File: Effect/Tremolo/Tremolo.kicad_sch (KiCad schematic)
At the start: 20 parts, among them J1 Conn_01x03_Pin, J2 Conn_01x03_Pin, Q1 PMV250, Q2 PMV250, U1 OPA1655

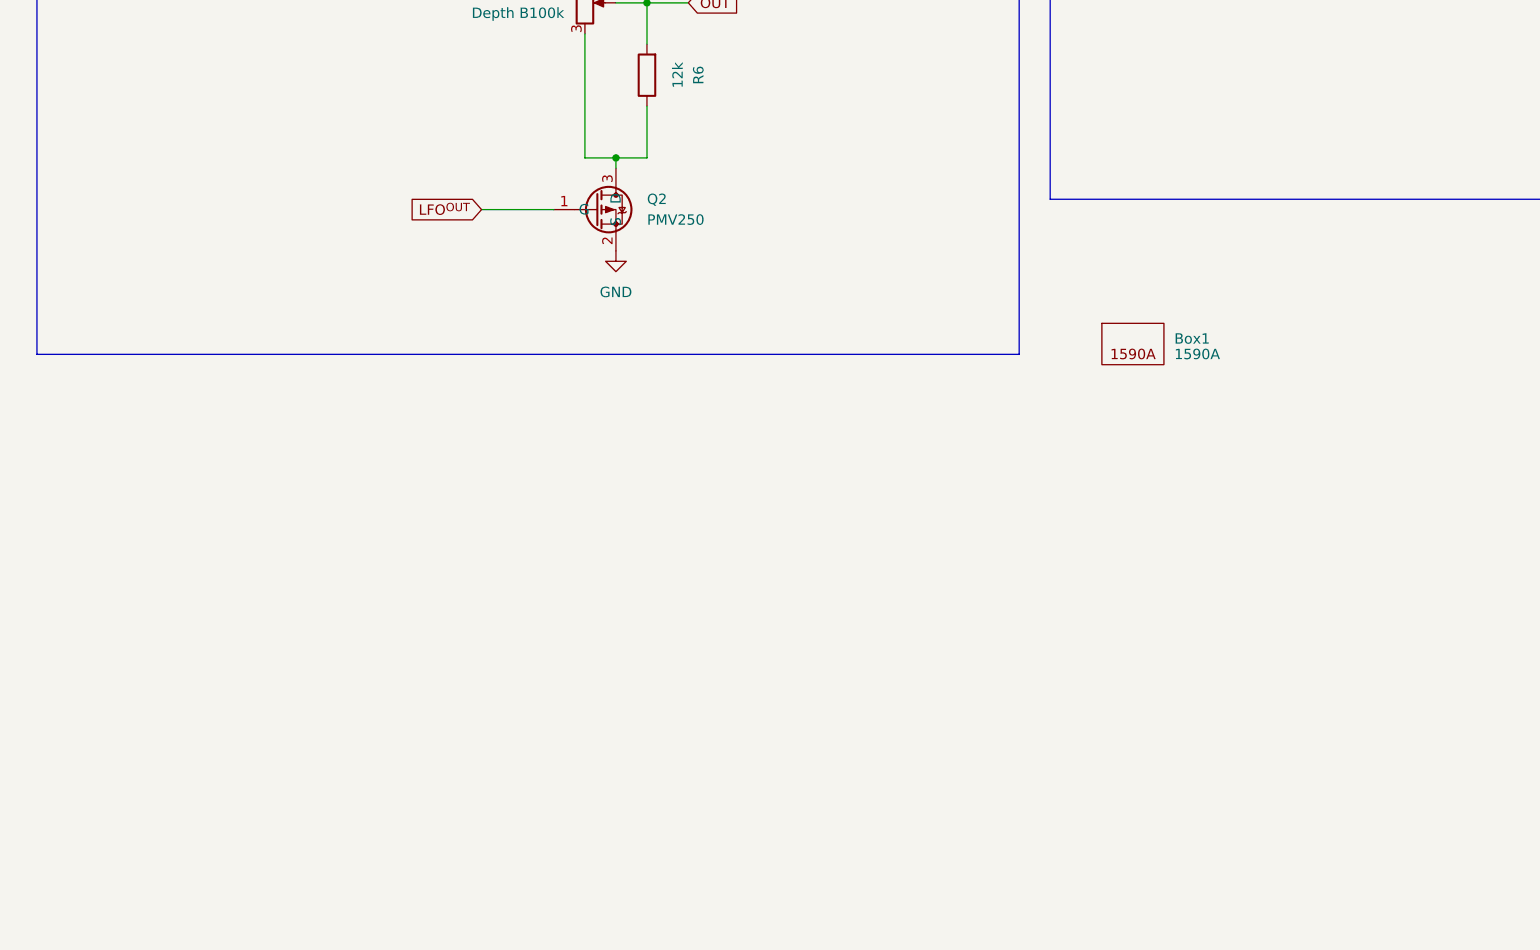
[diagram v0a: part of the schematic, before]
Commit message: Tremolo: Add SPICE simulation elements
The voltage sources and the model of RV2 are located outside / below the
sheet since they are not part of the "real" circuit. Set the voltage
sources and RV2 simulation-placeholder resister as being excluded from
the BOM and board. Set RV2 as excluded from the simulation since R7 and
R8 take its place.

Add another global label at the drain of Q2 so the two resistors that
model RV2 can be placed outside of the sheet.

Use 210mV @ 344Hz for the input per Linus's own testing.

The SPICE model for OPA1655 and PMV250 are expected to be inside the
Tremolo project directory, named "OPA1655.LIB" and
"PMV250EPEA_22_5_2013.lib" as they are from the manufacturers' websites.

Signed-off-by: Eric Kuzmenko <eric.n.kuzmenko@gmail.com>
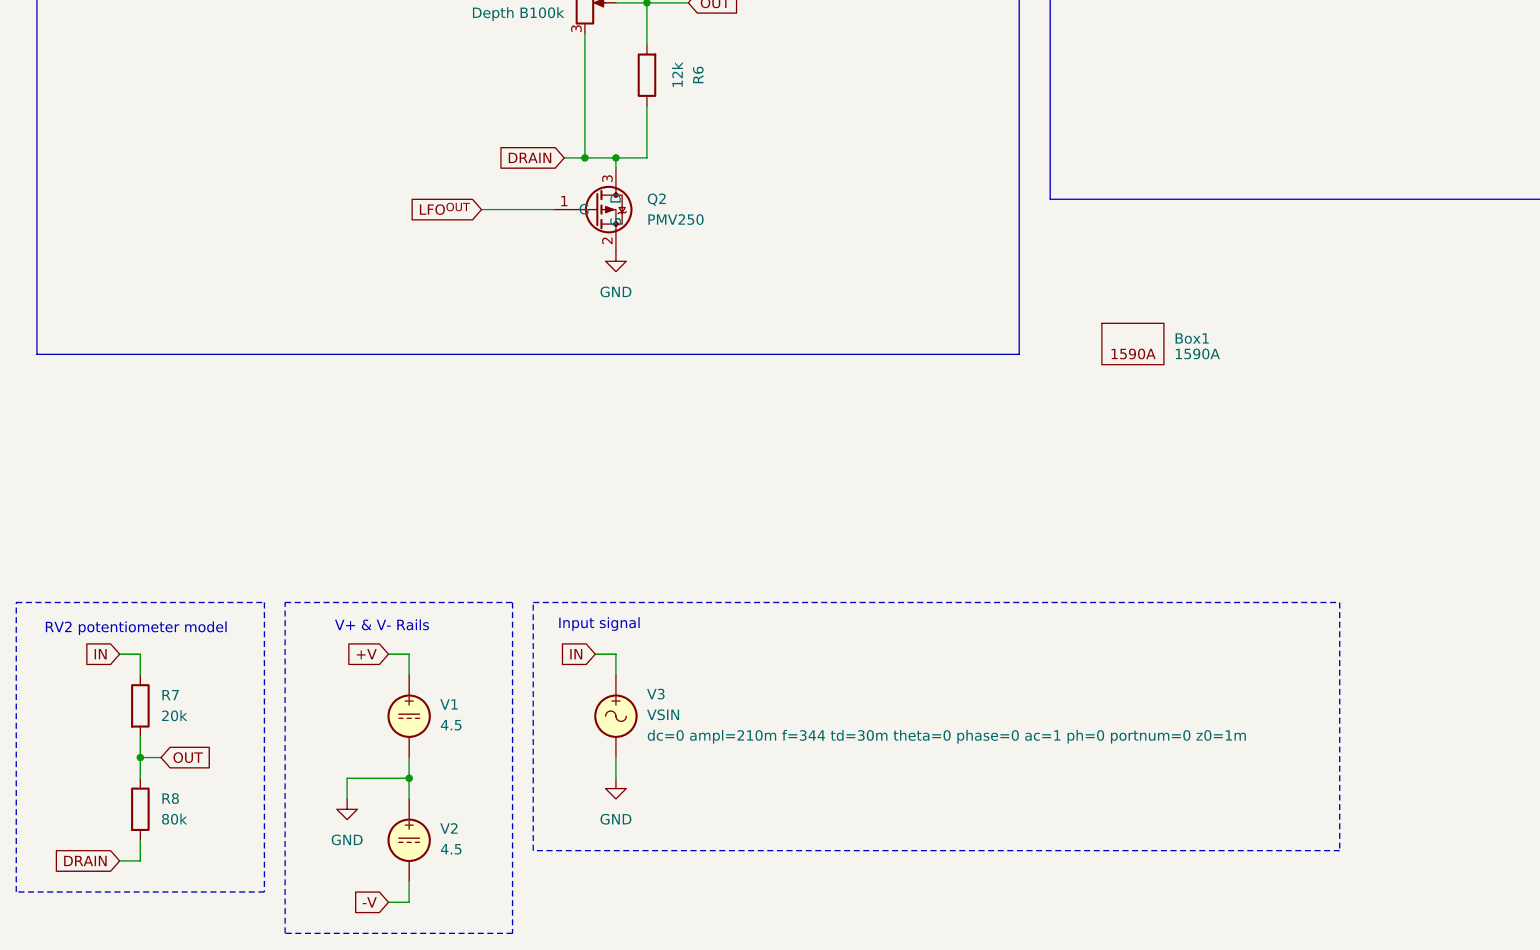
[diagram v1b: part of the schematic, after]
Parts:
- added R7: 20k, symbol Device:R
- added R8: 80k, symbol Device:R
- added V1, V2: 4.5, symbol Simulation_SPICE:VDC
- added V3: VSIN, symbol Simulation_SPICE:VSIN
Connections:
- net +V: now also V1.1
- net -V: now also V2.2
- net GND: now also V1.2, V2.1, V3.2
- net IN: now also R7.1, V3.1
- net OUT: now also R7.2, R8.1
- net DRAIN: now reaches Q2.3 (D), R6.1, RV2.3
- net DRAIN: now also R8.2
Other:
- note added: "Input signal"
- note added: "RV2 potentiometer model"
- note added: "V+ & V- Rails"

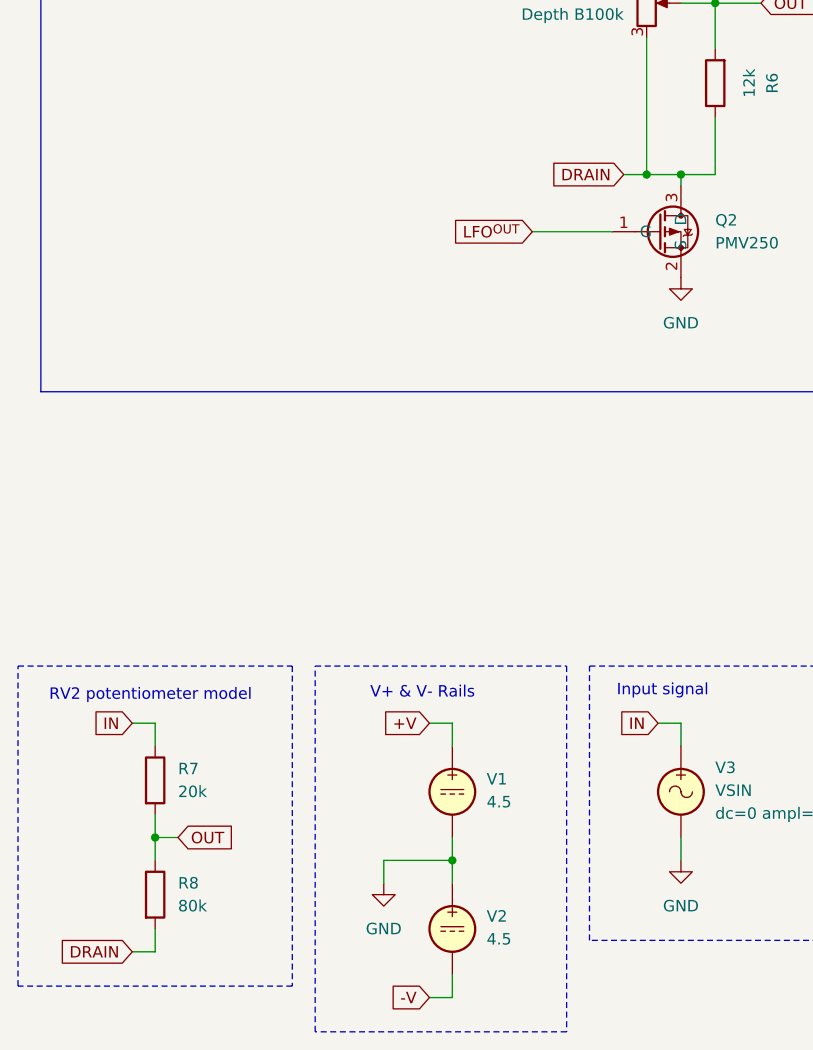
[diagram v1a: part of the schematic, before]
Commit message: Tremolo: Use the potentiometer SPICE model for RV1 and RV2
Get rid of R7 and R8 since the built-in potentiometer device SPICE
device type works just fine.

Signed-off-by: Eric Kuzmenko <eric.n.kuzmenko@gmail.com>
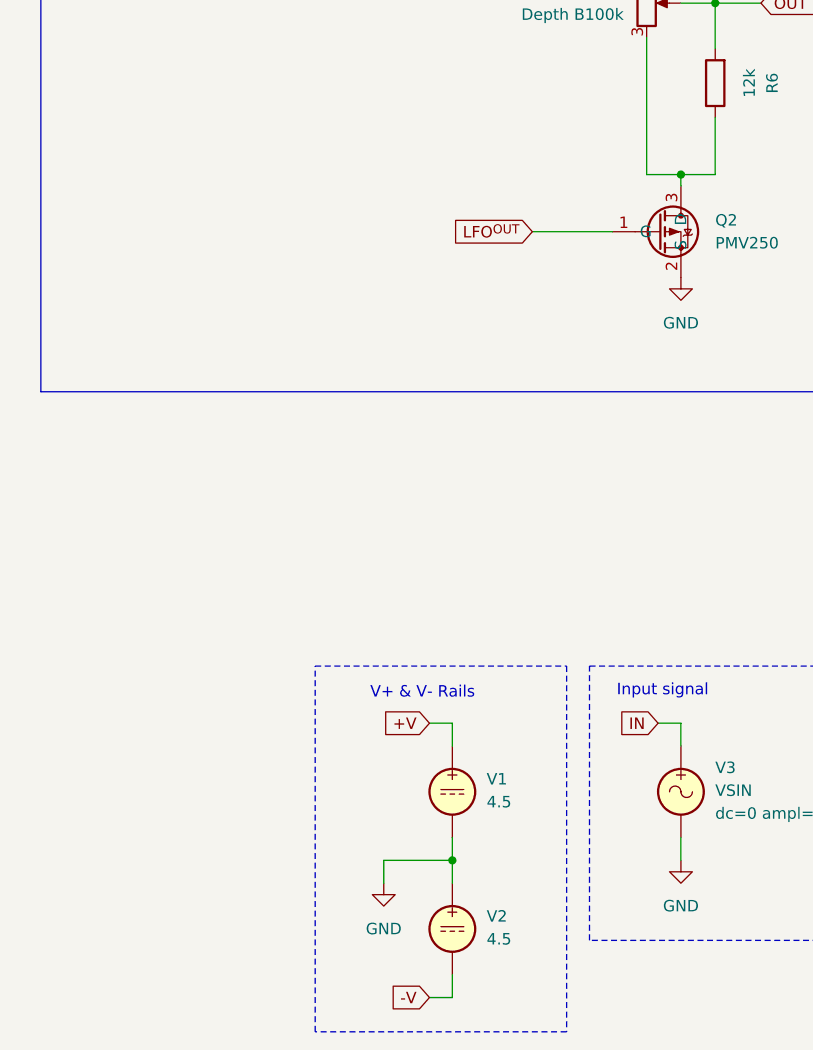
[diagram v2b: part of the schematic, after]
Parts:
- removed R7: 20k, symbol Device:R
- removed R8: 80k, symbol Device:R
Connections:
- net DRAIN: no longer names the net of Q2.3 (D), R6.1, RV2.3
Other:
- note removed: "RV2 potentiometer model"
